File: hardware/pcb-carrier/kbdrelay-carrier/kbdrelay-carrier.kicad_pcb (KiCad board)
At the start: 2 copper layers, 120 x 55 mm, 20 parts, among them J1 UART_KBD, J2 UART_TGT, J3 5V_IN, U1 ESP32-S3-Zero, U2 ESP32-S3-Zero

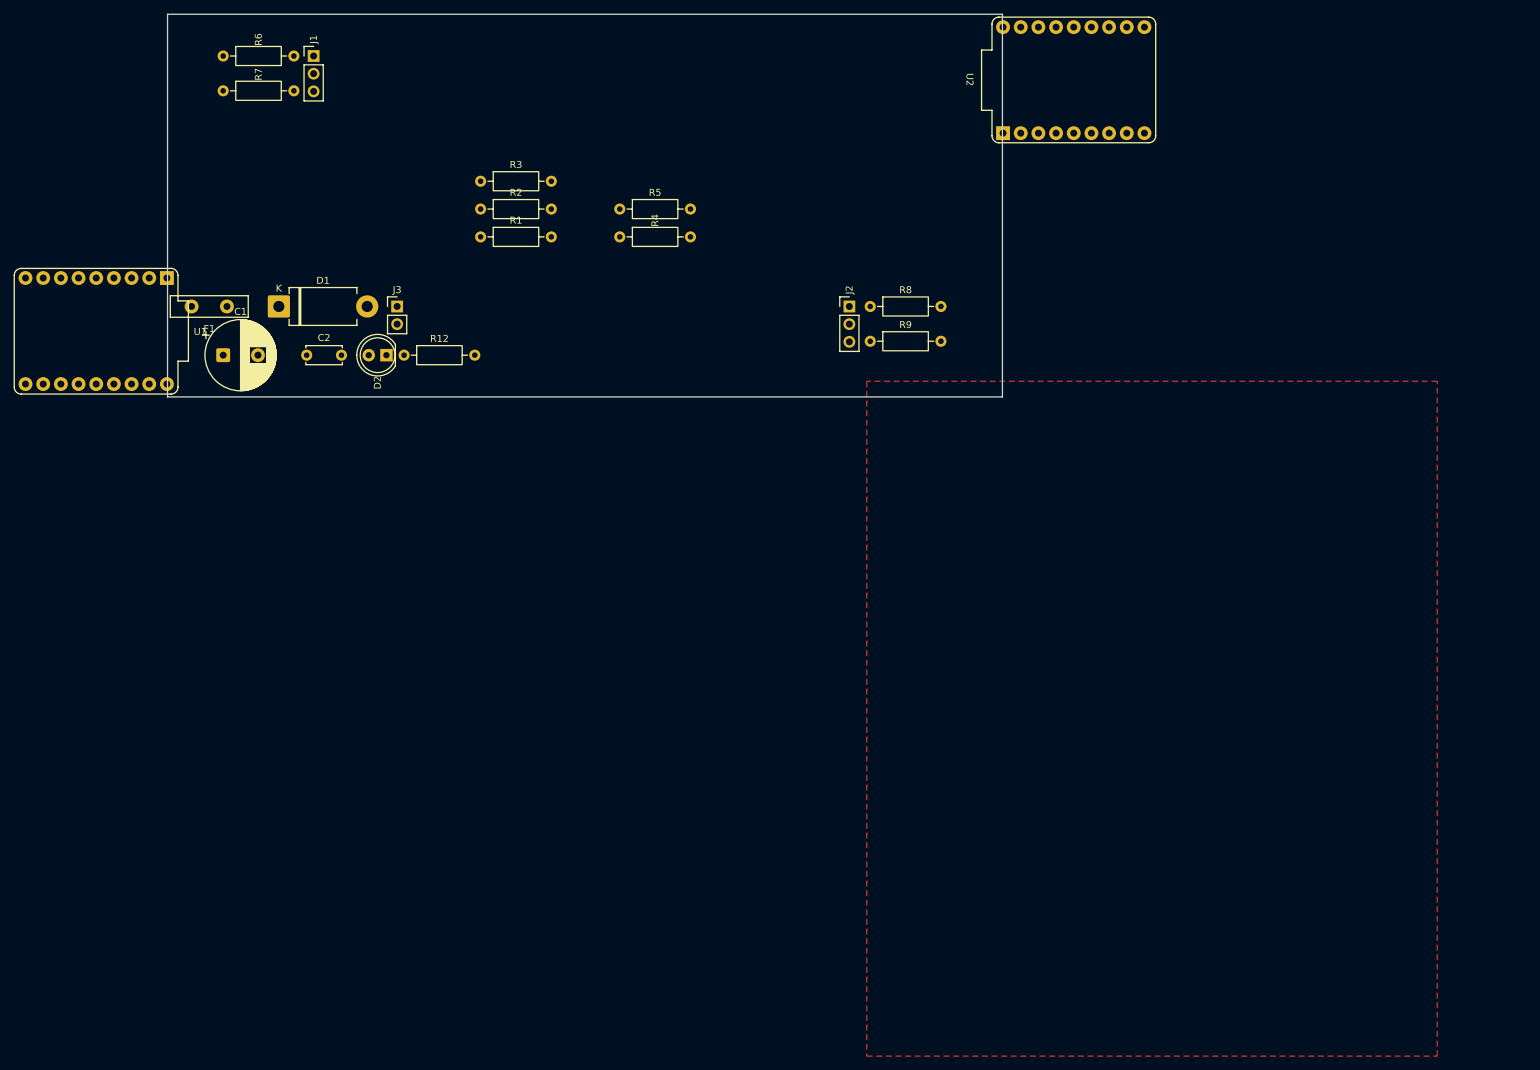
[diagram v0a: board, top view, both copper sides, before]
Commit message: feat(pcb): complete single-layer layout — 88x55 mm, zero jumpers, DRC-clean
Picks up the paused T-004 layout work.

Fixes a placement bug that made the board unbuildable: both ESP32-S3-Zero
modules sat entirely off the board (U1 pads at x -20..0, U2 at 122..140 on a
0-120 mm board). The anchors were right; the rotations were inverted (U1 had
270 where it needs 90, U2 the reverse). The old DRC's "4 copper-edge corner
artifacts" were this. Every discrete had been placed around the intended pad
grid, so only the two rotations needed correcting.

Layout is now scripted and idempotent rather than hand-edited:
- place.py  — placement table, outline, 4x M3 holes, silkscreen, mirrored
              BOTTOM label on B.Cu, board centred on the A4 sheet
- route.py  — single-layer B.Cu maze router (per-trace-width obstacle grids,
              randomized-restart net ordering), GND pour with solid pad
              connections, and a fill-verify-repair pass for the pour

Result: 88 x 55 mm (was 120 x 55 — the extra width was dead space), 100%
routed on B.Cu, zero wire jumpers, zero unconnected, and no clearance, short,
crossing or copper-edge DRC violations. Remaining DRC output is cosmetic:
silk clipped by the intentional USB-C overhang notches, courtyard overlaps in
the dense THT power cluster, and pre-existing lib_footprint_mismatch.

Also retracts the "a crossing-free SPI link is topologically impossible"
claim: it ignored routing around a module and under its body between the two
pad rows. Neither parked escape hatch (flipping U2 to the back layer,
reversing TGT's SPI pin order in firmware) is needed.

Notable near-misses caught along the way: the GND pour silently stranded
C1.2, C2.2 and U2.2 on isolated islands (fixed with GND-only keep-clear
channels); thermal reliefs starved GND pads; and square pin-1 pads need a
sqrt(2) clearance radius, not a circular one.

Design deviations recorded in design.md; T-001..T-004 checked off.
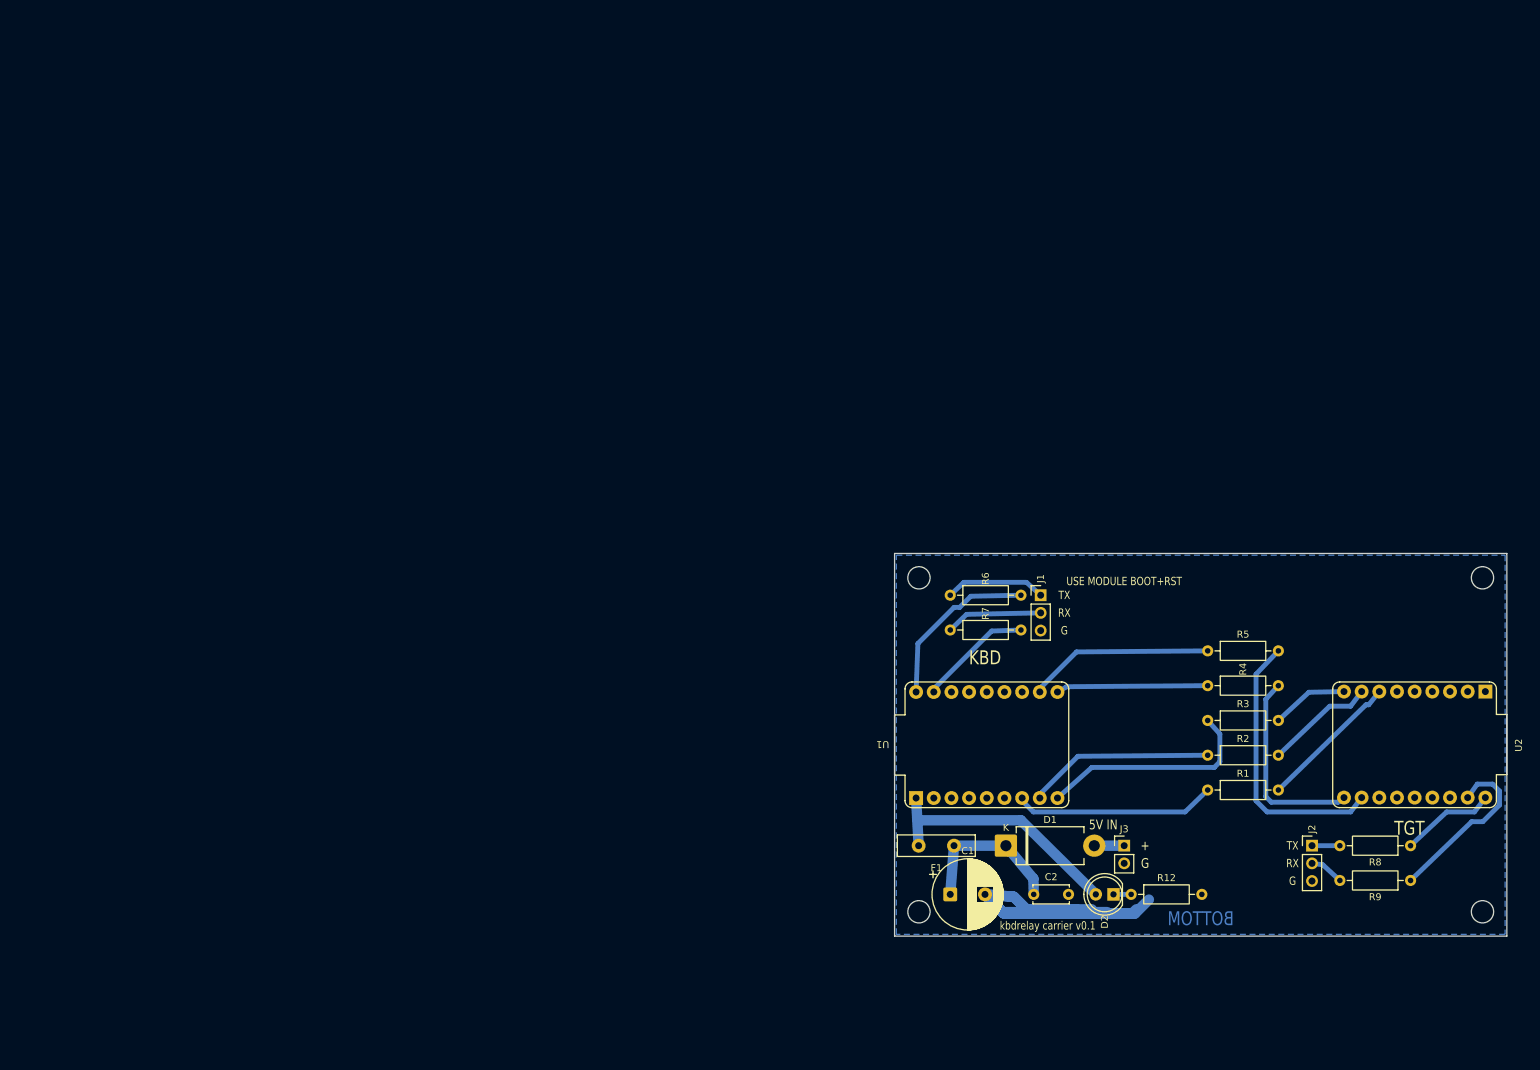
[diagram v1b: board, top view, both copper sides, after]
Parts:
- added H1: MountingHole_3.2mm_M3, MountingHole_3.2mm_M3, F.Cu at (108.0, 81.0)
- added H2: MountingHole_3.2mm_M3, MountingHole_3.2mm_M3, F.Cu at (189.0, 81.0)
- added H3: MountingHole_3.2mm_M3, MountingHole_3.2mm_M3, F.Cu at (108.0, 129.0)
- added H4: MountingHole_3.2mm_M3, MountingHole_3.2mm_M3, F.Cu at (189.0, 129.0)
- moved R1 131.3 mm to (149.5, 111.5)
- moved R2 130.7 mm to (149.5, 106.5)
- moved C1 130.1 mm to (112.5, 126.5)
- moved C2 130.1 mm to (124.5, 126.5)
- moved D1 130.1 mm to (120.5, 119.5)
- moved D2 130.1 mm to (136.0, 126.5)
- moved F1 130.1 mm to (110.5, 119.5)
- moved J1 130.1 mm to (125.5, 83.5)
- moved J3 130.1 mm to (137.5, 119.5)
- moved R12 130.1 mm to (138.5, 126.5)
- moved R3 130.1 mm to (149.5, 101.5)
- moved R6 130.1 mm to (112.5, 83.5)
- moved R7 130.1 mm to (112.5, 88.5)
- moved U1 130.1 mm to (106.0, 114.0), turned to 90 degrees
- moved R8 109.7 mm to (178.7, 119.5), turned to 180 degrees
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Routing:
- net GND: track 0.00 -> 118.2 mm
- net /DRDY_TGT: track 0.00 -> 39.7 mm
- net /+5V_KBD: track 0.00 -> 36.8 mm
- net Net-(U1-GPIO6): track 0.00 -> 32.0 mm
- net Net-(U1-GPIO4): track 0.00 -> 28.9 mm
- net /CS_TGT: track 0.00 -> 28.5 mm
- net Net-(U1-GPIO5): track 0.00 -> 26.9 mm
- net /DRDY_KBD: track 0.00 -> 26.7 mm
- net Net-(U2-RX): track 0.00 -> 25.2 mm
- net Net-(U1-TX): track 0.00 -> 24.6 mm
- net /+5V_PROT: track 0.00 -> 22.9 mm
- net /CS_KBD: track 0.00 -> 21.8 mm
- net Net-(U2-GPIO4): track 0.00 -> 20.4 mm
- net Net-(U1-RX): track 0.00 -> 16.4 mm
- net Net-(U2-GPIO5): track 0.00 -> 15.8 mm
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- added copper zone on B.Cu, net GND
- removed copper zone on F.Cu, net (none)
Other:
- board size 120 x 55 mm -> 88 x 55 mm
- board text added: "+"
- board text added: "5V IN"
- board text added: "BOTTOM"
- board text added: "G"
- board text added: "KBD"
- board text added: "RX"
- board text added: "TGT"
- board text added: "TX"
- board text added: "USE MODULE BOOT+RST"
- board text added: "kbdrelay carrier v0.1"
